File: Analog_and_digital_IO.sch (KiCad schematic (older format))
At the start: 113 parts

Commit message: Buttons complete
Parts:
- added C?: 1µF, Capacitor_SMD:C_0603_1608Metric_Pad1.08x0.95mm_HandSolder, symbol Device:C
- R? (x2): value 5,1K -> 10K
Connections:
- net GNDREF: now also C?.2
- net VDD_PER: now also C?.1
- net SKIP_N_UNLOADED_SOUD renamed SKIP_N_UNLOADED_BEEPER
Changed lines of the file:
@@
 $Descr A3 16535 11693
 encoding utf-8
-Sheet 7 9
+Sheet 7 10
 Title ""
 Date "2021-05-02"
@@
 AR Path="/60D8C564/60AC53E0" Ref="R?"  Part="1"
 F 0 "R?" V 13020 3620 50  0000 C CNN
-F 1 "5,1K" V 13210 3630 50  0000 C CNN
+F 1 "10K" V 13210 3630 50  0000 C CNN
 F 2 "Resistor_SMD:R_0805_2012Metric_Pad1.20x1.40mm_HandSolder" V 13040 3660 50  0001 C CNN
 F 3 "~" H 13110 3660 50  0001 C CNN
@@
 AR Path="/60D8C564/60C3EDA2" Ref="R?"  Part="1"
 F 0 "R?" V 13020 4860 50  0000 C CNN
-F 1 "5,1K" V 13210 4870 50  0000 C CNN
+F 1 "10K" V 13210 4870 50  0000 C CNN
 F 2 "Resistor_SMD:R_0805_2012Metric_Pad1.20x1.40mm_HandSolder" V 13040 4900 50  0001 C CNN
 F 3 "~" H 13110 4900 50  0001 C CNN
@@
 	12750 4900 12960 4900
 Text HLabel 12750 4900 0    50   Input ~ 0
-SKIP_N_UNLOADED_SOUD
+SKIP_N_UNLOADED_BEEPER
 $Comp
 L Device:Speaker_Crystal LS?
@@
 $EndComp
 Wire Wire Line
-	13560 4290 13560 4440
+	13560 4290 13560 4310
 Wire Wire Line
 	14760 1740 15280 1740
@@
 Text HLabel 11540 2040 0    50   Input ~ 0
 LEVEL_SWITCH_AC
+$Comp
+L Device:C C?
+U 1 1 60CE87D0
+P 13320 4460
+AR Path="/60CE87D0" Ref="C?"  Part="1"
+AR Path="/60A03F8A/60CE87D0" Ref="C?"  Part="1"
+AR Path="/60D8C564/60CE87D0" Ref="C?"  Part="1"
+F 0 "C?" H 13040 4500 50  0000 L CNN
+F 1 "1µF" H 13040 4420 50  0000 L CNN
+F 2 "Capacitor_SMD:C_0603_1608Metric_Pad1.08x0.95mm_HandSolder" H 13358 4310 50  0001 C CNN
+F 3 "http://www.farnell.com/datasheets/2710676.pdf" H 13320 4460 50  0001 C CNN
+F 4 "?????? CL10B105KA8NNNC" H 13320 4460 50  0001 C CNN "Type"
+	1    13320 4460
+	1    0    0    -1
+$EndComp
+$Comp
+L power:GNDREF #PWR?
+U 1 1 60CE9784
+P 13320 4610
+AR Path="/60CE9784" Ref="#PWR?"  Part="1"
+AR Path="/60A03F8A/60CE9784" Ref="#PWR?"  Part="1"
+AR Path="/608C8099/60CE9784" Ref="#PWR?"  Part="1"
+AR Path="/60D8C564/60CE9784" Ref="#PWR?"  Part="1"
+F 0 "#PWR?" H 13320 4360 50  0001 C CNN
+F 1 "GNDREF" V 13325 4482 50  0001 R CNN
+F 2 "" H 13320 4610 50  0001 C CNN
+F 3 "" H 13320 4610 50  0001 C CNN
+	1    13320 4610
+	1    0    0    -1
+$EndComp
+Wire Wire Line
+	13320 4310 13560 4310
+Connection ~ 13560 4310
+Wire Wire Line
+	13560 4310 13560 4440
 $EndSCHEMATC

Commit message: analog IO MCU pin named
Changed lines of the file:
@@
 Wire Wire Line
 	13560 4310 13560 4440
+Text Label 9050 2220 0    50   ~ 0
+PF12
+Text Label 9040 5280 0    50   ~ 0
+PF13
+Text Label 9120 8840 0    50   ~ 0
+PF5
+Text Label 7820 9740 0    50   ~ 0
+PF4
+Text Label 7560 3120 0    50   ~ 0
+PF11
+Text Label 7640 6180 0    50   ~ 0
+PF14
 $EndSCHEMATC

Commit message: analog IO MCU pin named
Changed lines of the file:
@@
 $EndComp
 Wire Wire Line
-	12750 3660 12960 3660
-Text HLabel 12750 3660 0    50   Input ~ 0
+	12250 3660 12960 3660
+Text HLabel 12250 3660 0    50   Input ~ 0
 SKIP_N_UNLOADED_REL
 $Comp
@@
 $EndComp
 Wire Wire Line
-	12750 4900 12960 4900
-Text HLabel 12750 4900 0    50   Input ~ 0
+	12270 4900 12960 4900
+Text HLabel 12270 4900 0    50   Input ~ 0
 SKIP_N_UNLOADED_BEEPER
 $Comp
@@
 Text Label 7640 6180 0    50   ~ 0
 PF14
+Text Label 12370 3660 0    50   ~ 0
+PD10
+Text Label 12370 4900 0    50   ~ 0
+PD14
+Text Label 15050 1740 0    50   ~ 0
+PD9
 $EndSCHEMATC

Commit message: v0.1
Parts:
- added J5: OSTTC020162, digikey-footprints:Term_Block_1x2_P5mm, symbol dk_Terminal-Blocks-Wire-to-Board:OSTTC020162
- added J7: OSTTC030162, digikey-footprints:Term_Block_1x3_P5mm, symbol dk_Terminal-Blocks-Wire-to-Board:OSTTC030162
- gave numbers to parts that had none: 114
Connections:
- net 220V_Phase: now also J5.1
- net LEVEL_SWITCH_AC: now also J5.2
- net SKIP_N_UNL_REL_NC: no longer names the net of RL1.2, RL1.7
- net SKIP_N_UNL_REL_NC: now also J7.3
- net SKIP_N_UNL_REL_NO: no longer names the net of RL1.4, RL1.5
- net SKIP_N_UNL_REL_NO: now also J7.2
- net SKIP_N_UNL_REL_SW: no longer names the net of RL1.3, RL1.6
- net SKIP_N_UNL_REL_SW: now also J7.1

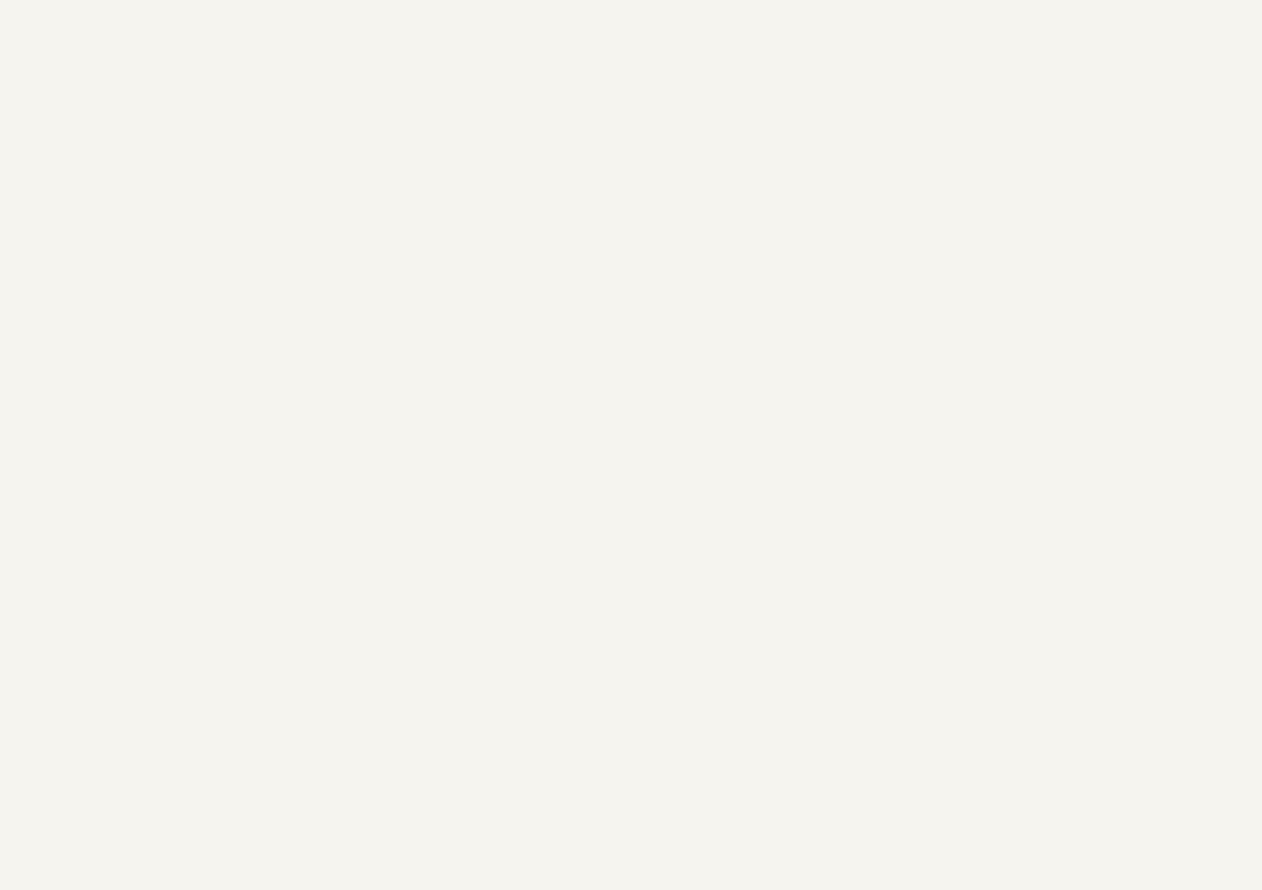
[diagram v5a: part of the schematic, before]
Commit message: v0.2 added ecoder inputs
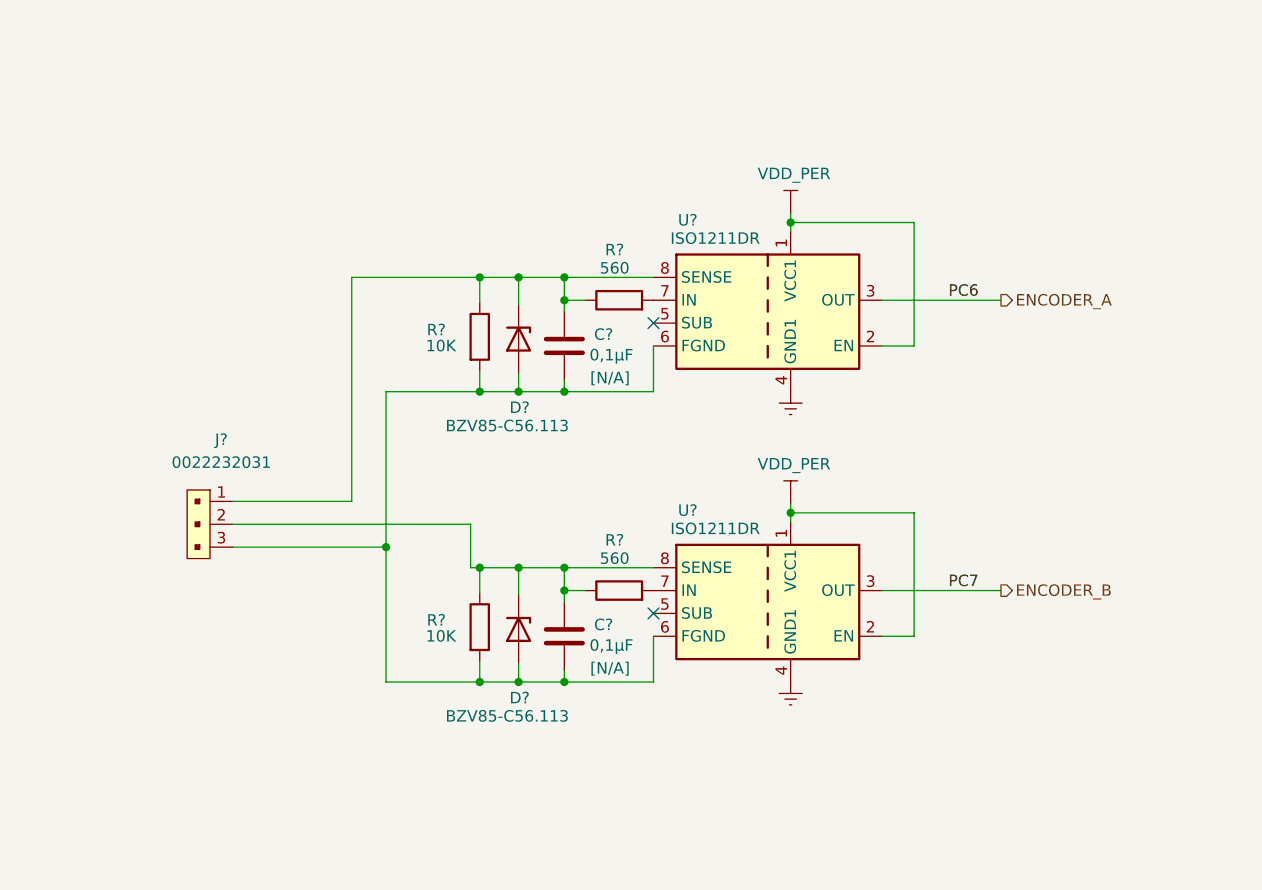
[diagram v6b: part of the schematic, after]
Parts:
- added C? (x2): 0,1µF, Capacitor_SMD:C_0603_1608Metric_Pad1.08x0.95mm_HandSolder, symbol Device:C
- added D? (x2): BZV85-C56.113, Diode_THT:D_DO-41_SOD81_P10.16mm_Horizontal, symbol Diode:1N47xxA
- added J?: 0022232031, digikey-footprints:PinHeader_1x3_P2.54mm_Drill1.02mm, symbol dk_Rectangular-Connectors-Headers-Male-Pins:0022232031
- added R? (x2): 560, Resistor_SMD:R_0805_2012Metric_Pad1.20x1.40mm_HandSolder, symbol Device:R
- added R? (x2): 10K, Resistor_SMD:R_0805_2012Metric_Pad1.20x1.40mm_HandSolder, symbol Device:R
- added U? (x2): ISO1211DR, Package_SO:SOIC-8_3.9x4.9mm_P1.27mm, symbol Isolator:ISO1211
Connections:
- net GNDREF: now also U?.4 (GND1), U?.4 (GND1)
- net VDD_PER: now also U?.1 (VCC1), U?.1 (VCC1), U?.2 (EN), U?.2 (EN)
- new net: C?.2, C?.2, D?.2 (A), D?.2 (A), J?.3, R?.2, R?.2, U?.6 (FGND), U?.6 (FGND)
- new net: R?.2, U?.7 (IN) (x2)
- new net: C?.1, D?.1 (K), J?.1, R?.1, R?.1, U?.8 (SENSE)
- new net: C?.1, D?.1 (K), J?.2, R?.1, R?.1, U?.8 (SENSE)
- new net ENCODER_A: U?.3 (OUT)
- new net ENCODER_B: U?.3 (OUT)
- no-connect marks 5 -> 7

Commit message: v0.3 changed sd_card holder
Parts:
- added C94, C95: 1µF, Capacitor_SMD:C_0603_1608Metric_Pad1.08x0.95mm_HandSolder, symbol Device:C
- C49: renamed from C54; footprint (none) -> Capacitor_Tantalum_SMD:CP_EIA-3216-10_Kemet-I; Type 593D106X9016A2TE3 -> 293D106X9035D2TE3
- C51: renamed from C56; footprint (none) -> Capacitor_Tantalum_SMD:CP_EIA-7343-30_AVX-N_Pad2.25x2.55mm_HandSolder; Type 593D106X9016A2TE3 -> 293D106X9035D2TE3
- C53: renamed from C58; footprint (none) -> Capacitor_Tantalum_SMD:CP_EIA-3216-10_Kemet-I
- C55: renamed from C60; Type CL10B105KA8NNNC -> C0603C104K5RACTU
- C56: renamed from C61; Type CL10B105KA8NNNC -> C1608X7R1H224K080AB
- C60: renamed from C65; footprint (none) -> Capacitor_Tantalum_SMD:CP_EIA-7343-30_AVX-N_Pad2.25x2.55mm_HandSolder; Type 593D106X9016A2TE3 -> 293D106X9035D2TE3
- C63: renamed from C68; Type CL10B105KA8NNNC -> C0603C104K5RACTU
- C64: renamed from C69; Type CL10B105KA8NNNC -> C1608X7R1H224K080AB
- C71: renamed from C75; footprint (none) -> Capacitor_Tantalum_SMD:CP_EIA-7343-30_AVX-N_Pad2.25x2.55mm_HandSolder; Type 593D106X9016A2TE3 -> 293D106X9035D2TE3
- C74: renamed from C77; Type CL10B105KA8NNNC -> C0603C104K5RACTU
- C75: renamed from C78; Type CL10B105KA8NNNC -> C1608X7R1H224K080AB
- D8: value D -> ES1G; footprint (none) -> Diode_SMD:D_SMA_Handsoldering
- R21, R24, R25, R39: footprint Resistor_SMD:R_0805_2012Metric_Pad1.20x1.40mm_HandSolder -> Resistor_THT:R_Axial_DIN0207_L6.3mm_D2.5mm_P10.16mm_Horizontal
- R51, R54: renamed from R?; footprint Resistor_SMD:R_0805_2012Metric_Pad1.20x1.40mm_HandSolder -> Resistor_THT:R_Axial_DIN0207_L6.3mm_D2.5mm_P10.16mm_Horizontal
- R55: renamed from R51; footprint Resistor_SMD:R_0805_2012Metric_Pad1.20x1.40mm_HandSolder -> Resistor_THT:R_Axial_DIN0207_L6.3mm_D2.5mm_P10.16mm_Horizontal
- gave numbers to parts that had none: 9
- renumbered C53 to C48, C55 to C50, C57 to C52, C59 to C54, C62 to C57, C63 to C58, C64 to C59, C66 to C61, C67 to C62, C70 to C65, C71 to C67, C72 to C68, C73 to C69, C74 to C70, C76 to C72, C79 to C76, D11 to D13, D12 to D14, J9 to J10, R50 to R52, R52 to R56, R53 to R57, R54 to R58, R55 to R59, R56 to R60, R57 to R61, R58 to R62, R59 to R63, R60 to R64, R61 to R65, U24 to U25, U25 to U27, U26 to U28, U27 to U29
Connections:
- net GNDREF: now also C94.2, C95.2
- net VDD_PER: now also C94.1, C95.1

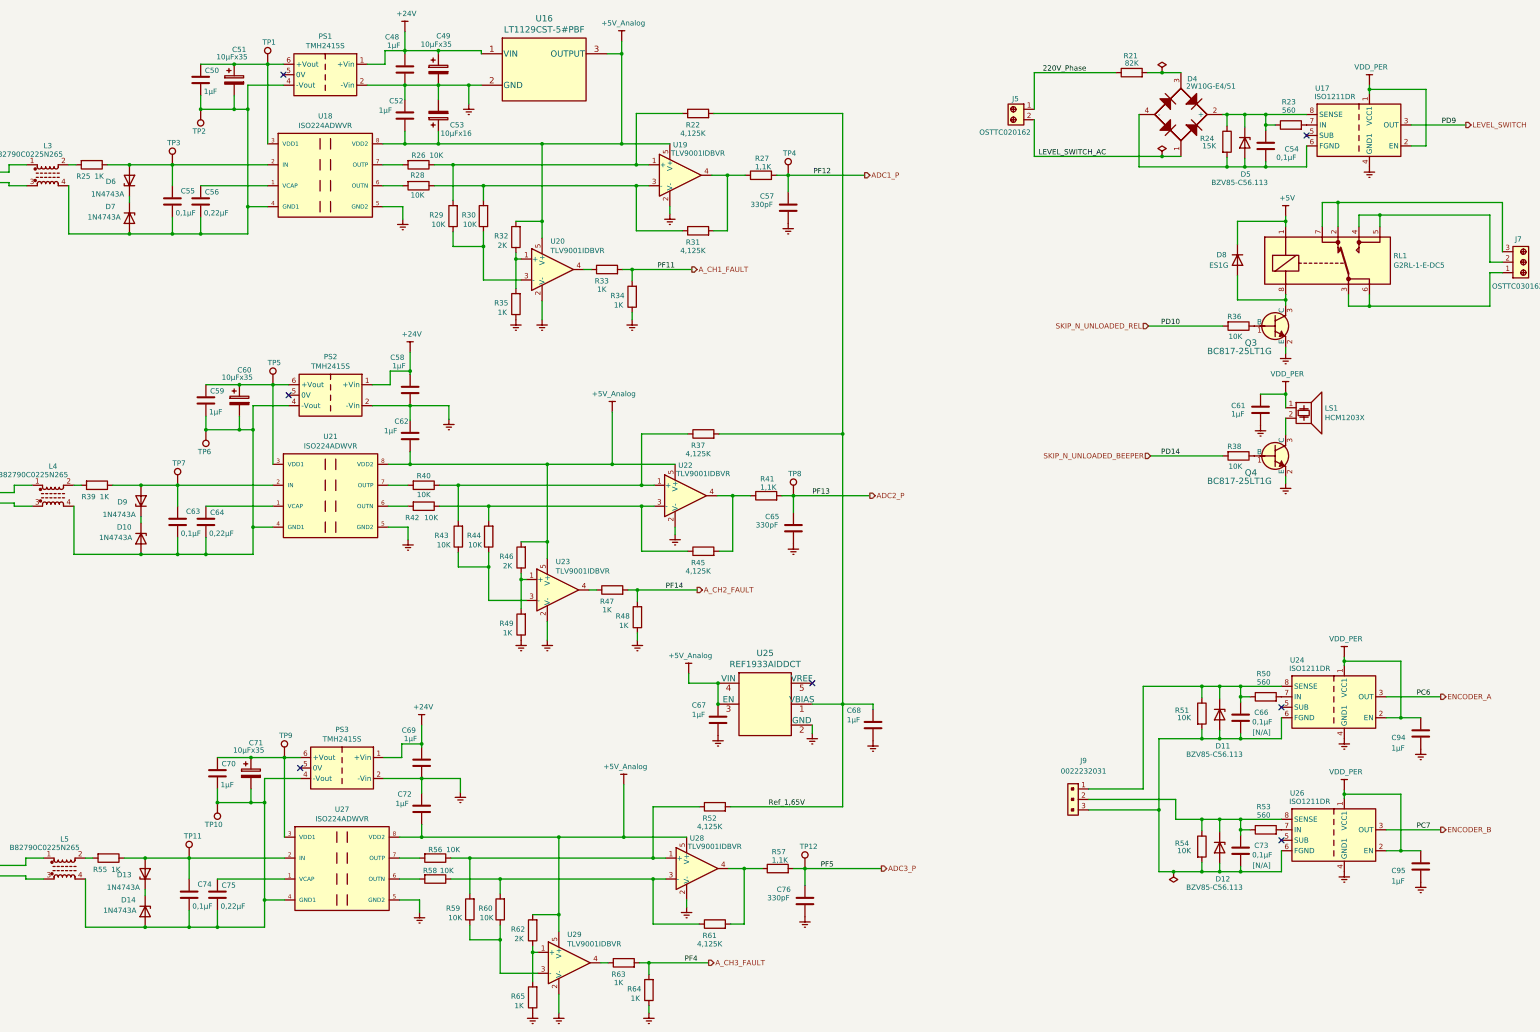
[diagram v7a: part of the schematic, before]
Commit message: footprints associations is done
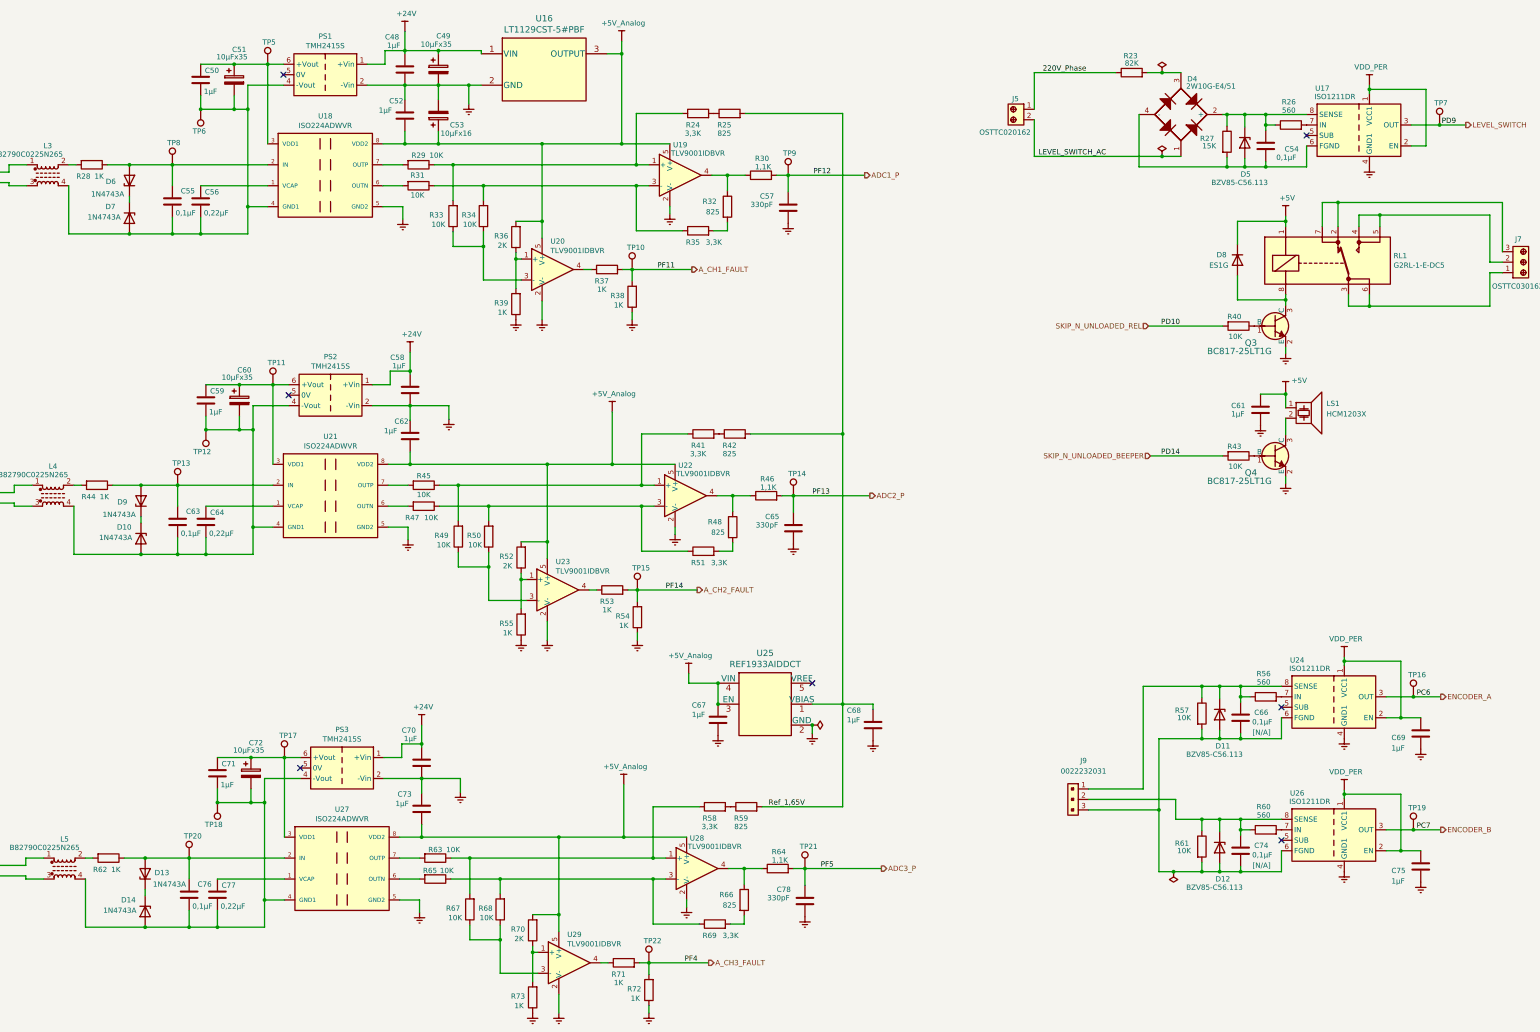
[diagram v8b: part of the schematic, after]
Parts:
- removed R37, R45, R52, R61: 4,125K, Resistor_SMD:R_0805_2012Metric_Pad1.20x1.40mm_HandSolder, symbol Device:R
- added R25, R32, R42, R48, R59, R66: 825, Resistor_SMD:R_0805_2012Metric_Pad1.20x1.40mm_HandSolder, symbol Device:R
- added R41, R51, R58, R69: 3,3K, Resistor_SMD:R_0805_2012Metric_Pad1.20x1.40mm_HandSolder, symbol Device:R
- added TP10, TP15, TP16, TP19, TP22, TP7: TestPoint, TestPoint:TestPoint_Pad_D1.5mm, symbol Connector:TestPoint
- C49: footprint Capacitor_Tantalum_SMD:CP_EIA-3216-10_Kemet-I -> Capacitor_Tantalum_SMD:CP_EIA-7343-30_AVX-N_Pad2.25x2.55mm_HandSolder
- C54, C66: Type CL10B105KA8NNNC -> CL10B104KC8NNNC
- C57: Type CL10B105KA8NNNC -> GRM188R71H331KA01D
- C74: renamed from C73; Type CL10B105KA8NNNC -> CL10B104KC8NNNC
- L3, L4, L5: footprint Inductor_SMD:L_Wuerth_WE-DD-Typ-L-Typ-XL-Typ-XXL -> Inductor_SMD:L_CommonMode_Delevan_4222
- LS1: footprint (none) -> Buzzer_Beeper:Buzzer_12x9.5RM7.6
- R24: renamed from R22; value 4,125K -> 3,3K
- R35: renamed from R31; value 4,125K -> 3,3K
- TP11: renamed from TP5; footprint (none) -> TestPoint:TestPoint_Pad_D1.5mm
- TP12: renamed from TP6; footprint (none) -> TestPoint:TestPoint_Pad_D1.5mm
- TP13: renamed from TP7; footprint (none) -> TestPoint:TestPoint_Pad_D1.5mm
- TP14: renamed from TP8; footprint (none) -> TestPoint:TestPoint_Pad_D1.5mm
- TP17: renamed from TP9; footprint (none) -> TestPoint:TestPoint_Pad_D1.5mm
- TP18: renamed from TP10; footprint (none) -> TestPoint:TestPoint_Pad_D1.5mm
- TP20: renamed from TP11; footprint (none) -> TestPoint:TestPoint_Pad_D1.5mm
- TP21: renamed from TP12; footprint (none) -> TestPoint:TestPoint_Pad_D1.5mm
- TP5: renamed from TP1; footprint (none) -> TestPoint:TestPoint_Pad_D1.5mm
- TP6: renamed from TP2; footprint (none) -> TestPoint:TestPoint_Pad_D1.5mm
- TP8: renamed from TP3; footprint (none) -> TestPoint:TestPoint_Pad_D1.5mm
- TP9: renamed from TP4; footprint (none) -> TestPoint:TestPoint_Pad_D1.5mm
- U18, U21, U27: footprint Texas_Instruments-DWV0008A-0-0-* -> SVIELCOM:Texas_Instruments-DWV0008A-0-0-IPC_A
- renumbered C94 to C69, C69 to C70, C70 to C71, C71 to C72, C72 to C73, C95 to C75, C74 to C76, C75 to C77, C76 to C78, R21 to R23, R23 to R26, R24 to R27, R25 to R28, R26 to R29, R27 to R30, R28 to R31, R29 to R33, R30 to R34, R32 to R36, R33 to R37, R34 to R38, R35 to R39, R36 to R40, R38 to R43, R39 to R44, R40 to R45, R41 to R46, R42 to R47, R43 to R49, R44 to R50, R46 to R52, R47 to R53, R48 to R54, R49 to R55, R50 to R56, R51 to R57, R53 to R60, R54 to R61, R55 to R62, R56 to R63, R57 to R64, R58 to R65, R59 to R67, R60 to R68, R62 to R70, R63 to R71, R64 to R72, R65 to R73
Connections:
- net +5V: now also C61.1, LS1.1
- net A_CH1_FAULT: now also TP10.1
- net A_CH2_FAULT: now also TP15.1
- net A_CH3_FAULT: now also TP22.1
- net ENCODER_A: now also TP16.1
- net ENCODER_B: now also TP19.1
- net LEVEL_SWITCH: now also TP7.1
- net Ref_1,65V: now also R25.2, R42.2, R59.2; no longer R24.2
- net VDD_PER: no longer C61.1, LS1.1
- net at R30.1, U19.4: now also R32.1; no longer R35.2
- net at R45.1, R49.2, U22.1 (+): now also R41.1
- net at R47.1, R50.2, U22.3 (-): now also R51.1
- net at R46.1, U22.4: now also R48.1
- net at R63.1, R67.2, U28.1 (+): now also R58.1
- net at R65.1, R68.2, U28.3 (-): now also R69.1
- net at R64.1, U28.4: now also R66.1
- new net: R32.2, R35.2
- new net: R24.2, R25.1
- new net: R41.2, R42.1
- new net: R58.2, R59.1
- new net: R48.2, R51.2
- new net: R66.2, R69.2
